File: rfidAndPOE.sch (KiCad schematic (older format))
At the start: 113 parts, among them J1 0813-1X1T-57-F, P1 PoE-, P2 PoE+, P3 GND, P4 +5V, P5 +12V, P6 +3V3, Q1 Si3440DV, NFET, Q2 MMBTA42, Q3 2N7002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

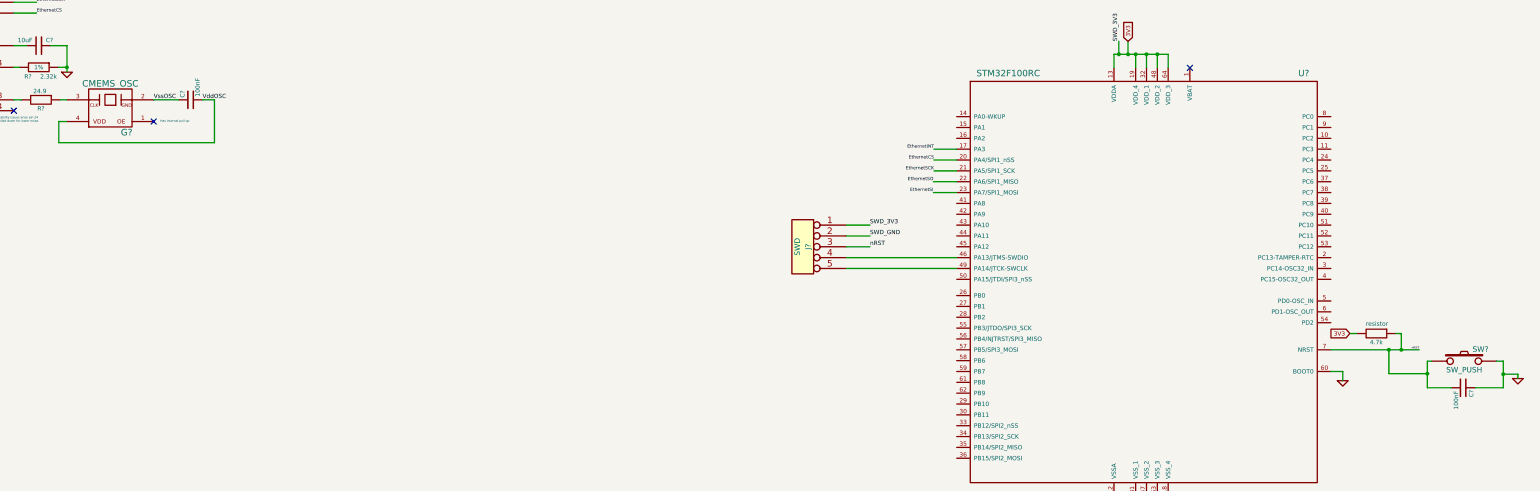
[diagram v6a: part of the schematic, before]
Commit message: Added 24MHz oscillator to the micro.
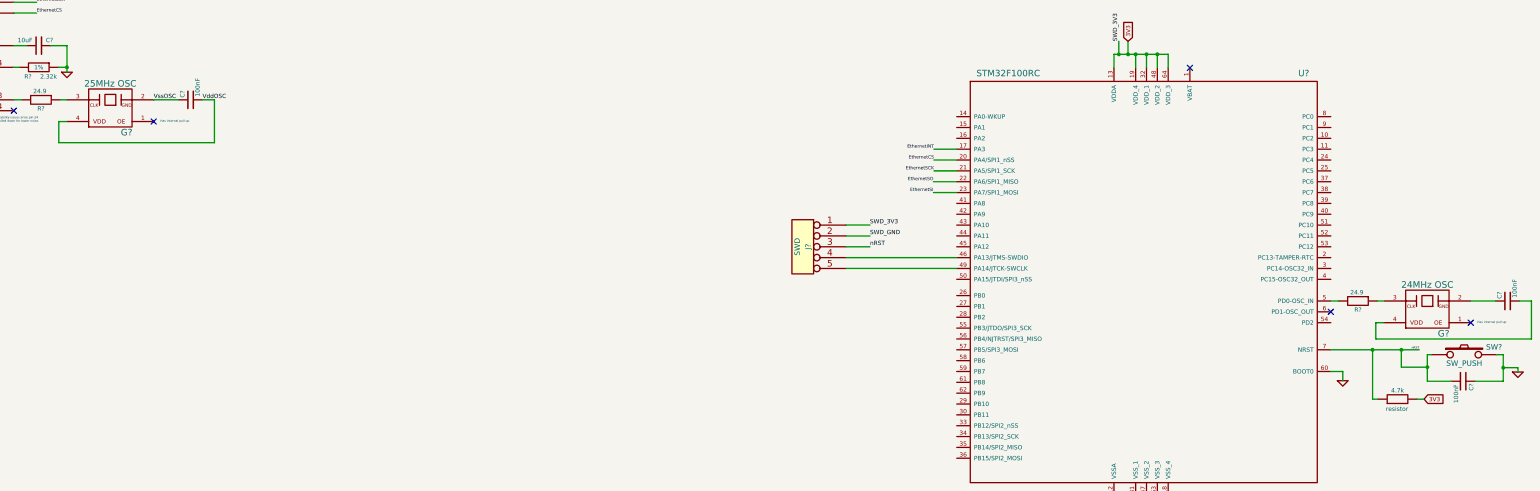
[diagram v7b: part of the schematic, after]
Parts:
- added C?: 100nF, SMD_Packages:SM0603, symbol capacitor
- added G?: 24MHz OSC, symbol CMEMS_OSC
- added R?: 24.9, SMD_Packages:SM0603, symbol resistor
- G?: value CMEMS_OSC -> 25MHz OSC
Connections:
- net at U?.5 (PD0-OSC_IN): now also R?.2
- new net: C?.1, G?.2 (GND)
- new net: C?.2, G?.4 (VDD)
- new net: G?.3 (CLK), R?.1
- no-connect marks 6 -> 8
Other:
- moved on the sheet: 4.7k, C?, SW?
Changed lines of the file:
@@
 P 7190 7920
 F 0 "G?" H 7040 8020 60  0000 C CNN
-F 1 "CMEMS_OSC" H 7190 7570 60  0000 C CNN
+F 1 "25MHz OSC" H 7190 7570 60  0000 C CNN
 F 2 "" H 7190 7720 60  0000 C CNN
 F 3 "" H 7190 7720 60  0000 C CNN
@@
 	16490 11465 16490 11570
 Connection ~ 16490 11465
-Text GLabel 18620 9875 0    39   Input ~ 0
+Text GLabel 19305 10480 2    39   Input ~ 0
 3V3
 $Comp
 L resistor 4.7k
 U 1 1 53ADAD98
-P 18865 9875
-F 0 "4.7k" V 18945 9875 40  0000 C CNN
-F 1 "resistor" V 18775 9880 40  0000 C CNN
-F 2 "" V 18795 9875 30  0000 C CNN
-F 3 "" H 18865 9875 30  0000 C CNN
-	1    18865 9875
-	0    1    1    0
-$EndComp
-Wire Wire Line
-	18620 9875 18685 9875
-Wire Wire Line
-	19045 9875 19095 9875
-Wire Wire Line
-	19095 9875 19095 10025
+P 19060 10480
+F 0 "4.7k" V 19140 10480 40  0000 C CNN
+F 1 "resistor" V 18970 10485 40  0000 C CNN
+F 2 "" V 18990 10480 30  0000 C CNN
+F 3 "" H 19060 10480 30  0000 C CNN
+	1    19060 10480
+	0    -1   -1   0
+$EndComp
+Wire Wire Line
+	19305 10480 19240 10480
+Wire Wire Line
+	18880 10480 18830 10480
+Wire Wire Line
+	19095 10025 19095 10185
 Connection ~ 19095 10025
 $Comp
 L SW_PUSH SW?
 U 1 1 53ADE5C4
-P 19675 10130
-F 0 "SW?" H 19825 10240 50  0000 C CNN
-F 1 "SW_PUSH" H 19675 10050 50  0000 C CNN
-F 2 "" H 19675 10130 60  0000 C CNN
-F 3 "" H 19675 10130 60  0000 C CNN
-	1    19675 10130
+P 19675 10070
+F 0 "SW?" H 19950 10140 50  0000 C CNN
+F 1 "SW_PUSH" H 19675 9990 50  0000 C CNN
+F 2 "" H 19675 10070 60  0000 C CNN
+F 3 "" H 19675 10070 60  0000 C CNN
+	1    19675 10070
 	1    0    0    -1
 $EndComp
@@
 L capacitor C?
 U 1 1 53ADF873
-P 19665 10375
-F 0 "C?" H 19685 10450 40  0000 L CNN
-F 1 "100nF" H 19695 10310 40  0000 L CNN
-F 2 "" H 19703 10225 30  0000 C CNN
-F 3 "" H 19665 10375 60  0000 C CNN
-	1    19665 10375
+P 19665 10315
+F 0 "C?" H 19685 10390 40  0000 L CNN
+F 1 "100nF" H 19695 10250 40  0000 L CNN
+F 2 "" H 19703 10165 30  0000 C CNN
+F 3 "" H 19665 10315 60  0000 C CNN
+	1    19665 10315
 	0    1    1    0
 $EndComp
@@
 L GND #PWR?
 U 1 1 53ADFE84
-P 20170 10290
-F 0 "#PWR?" H 20170 10290 30  0001 C CNN
-F 1 "GND" H 20170 10220 30  0001 C CNN
-F 2 "" H 20170 10290 60  0000 C CNN
-F 3 "" H 20170 10290 60  0000 C CNN
-	1    20170 10290
-	1    0    0    -1
-$EndComp
-Wire Wire Line
-	19375 10130 19335 10130
-Wire Wire Line
-	19335 10130 19335 10375
-Wire Wire Line
-	19335 10375 19555 10375
-Wire Wire Line
-	19975 10130 20035 10130
-Wire Wire Line
-	20035 10130 20035 10375
-Wire Wire Line
-	20035 10375 19775 10375
-Wire Wire Line
-	20170 10290 20170 10250
-Wire Wire Line
-	20170 10250 20035 10250
-Connection ~ 20035 10250
-Wire Wire Line
-	18980 10025 18980 10245
-Wire Wire Line
-	18980 10245 19335 10245
-Connection ~ 19335 10245
-Connection ~ 18980 10025
+P 20170 10230
+F 0 "#PWR?" H 20170 10230 30  0001 C CNN
+F 1 "GND" H 20170 10160 30  0001 C CNN
+F 2 "" H 20170 10230 60  0000 C CNN
+F 3 "" H 20170 10230 60  0000 C CNN
+	1    20170 10230
+	1    0    0    -1
+$EndComp
+Wire Wire Line
+	19375 10070 19335 10070
+Wire Wire Line
+	19335 10070 19335 10315
+Wire Wire Line
+	19335 10315 19555 10315
+Wire Wire Line
+	19975 10070 20035 10070
+Wire Wire Line
+	20035 10070 20035 10315
+Wire Wire Line
+	20035 10315 19775 10315
+Wire Wire Line
+	20170 10230 20170 10190
+Wire Wire Line
+	20170 10190 20035 10190
+Connection ~ 20035 10190
+Wire Wire Line
+	19095 10185 19335 10185
+Connection ~ 19335 10185
 $Comp
 L GND #PWR?
@@
 Text Notes 16810 6160 0    20   ~ 0
 Put the 1uF cap near the analog supply\n and the digital supply near it.
+$Comp
+L capacitor C?
+U 1 1 53B12180
+P 20075 9575
+F 0 "C?" H 20095 9650 40  0000 L CNN
+F 1 "100nF" H 20105 9510 40  0000 L CNN
+F 2 "SMD_Packages:SM0603" H 20113 9425 30  0001 C CNN
+F 3 "" H 20075 9575 60  0000 C CNN
+	1    20075 9575
+	0    -1   -1   0
+$EndComp
+$Comp
+L CMEMS_OSC G?
+U 1 1 53B12187
+P 19335 9775
+F 0 "G?" H 19185 9875 60  0000 C CNN
+F 1 "24MHz OSC" H 19335 9425 60  0000 C CNN
+F 2 "" H 19335 9575 60  0000 C CNN
+F 3 "" H 19335 9575 60  0000 C CNN
+	1    19335 9775
+	-1   0    0    1
+$EndComp
+Wire Wire Line
+	18935 9775 18860 9775
+Wire Wire Line
+	19735 9575 19965 9575
+Wire Wire Line
+	18860 9775 18860 9925
+Wire Wire Line
+	18860 9925 20295 9925
+Wire Wire Line
+	20295 9925 20295 9575
+Wire Wire Line
+	20295 9575 20185 9575
+$Comp
+L resistor R?
+U 1 1 53B12195
+P 18695 9575
+F 0 "R?" V 18775 9575 40  0000 C CNN
+F 1 "24.9" V 18615 9565 40  0000 C CNN
+F 2 "SMD_Packages:SM0603" V 18625 9575 30  0001 C CNN
+F 3 "" H 18695 9575 30  0000 C CNN
+	1    18695 9575
+	0    1    1    0
+$EndComp
+Wire Wire Line
+	18445 9575 18515 9575
+Wire Wire Line
+	18875 9575 18935 9575
+NoConn ~ 19735 9775
+Text Notes 19795 9790 0    20   ~ 0
+Has internal pull up
+NoConn ~ 18445 9675
+Wire Wire Line
+	18830 10480 18830 10025
+Connection ~ 18830 10025
 $EndSCHEMATC

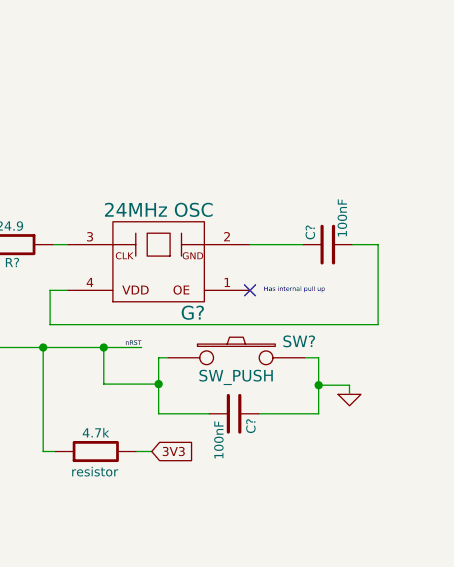
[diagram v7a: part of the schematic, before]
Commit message: Started schematic symbol for the RFID/NFC chip (CR95HF). Also added a note to check other symbols for belly pads. Almost forgot to do that!
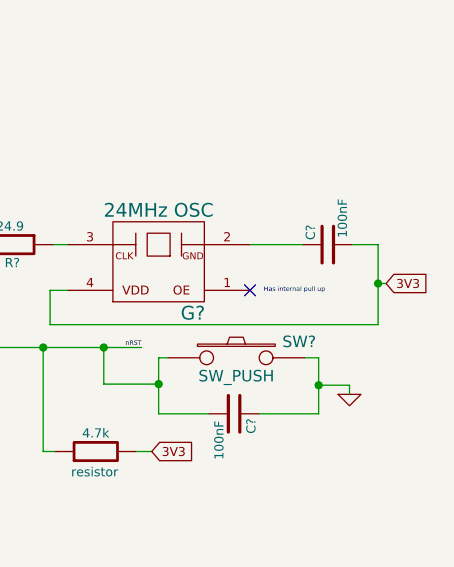
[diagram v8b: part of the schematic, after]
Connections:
- net 3V3: now also C?.2, G?.4 (VDD)
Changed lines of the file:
@@
 	18830 10480 18830 10025
 Connection ~ 18830 10025
+Text GLabel 20330 9745 2    39   Input ~ 0
+3V3
+Wire Wire Line
+	20330 9745 20295 9745
+Connection ~ 20295 9745
 $EndSCHEMATC
